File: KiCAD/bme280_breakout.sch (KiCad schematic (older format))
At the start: 8 parts, among them J1 2JUMPER, J2 2JUMPER, P1 CONN_4, U1 BME280

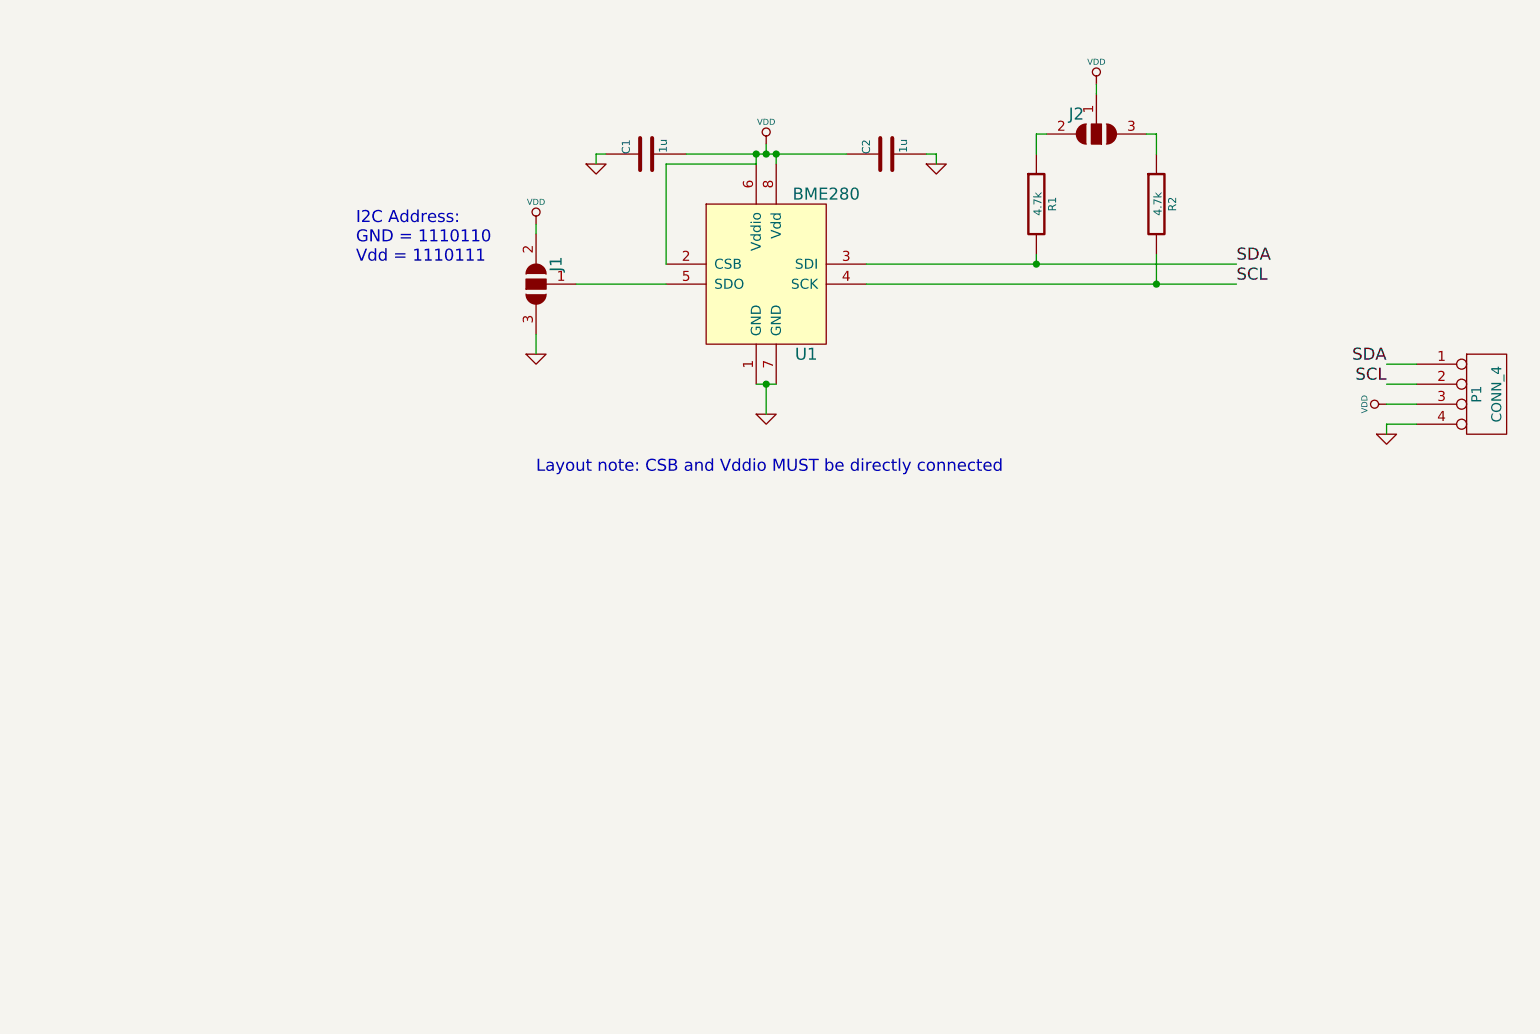
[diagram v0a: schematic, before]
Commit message: Update documentation and clean up repo
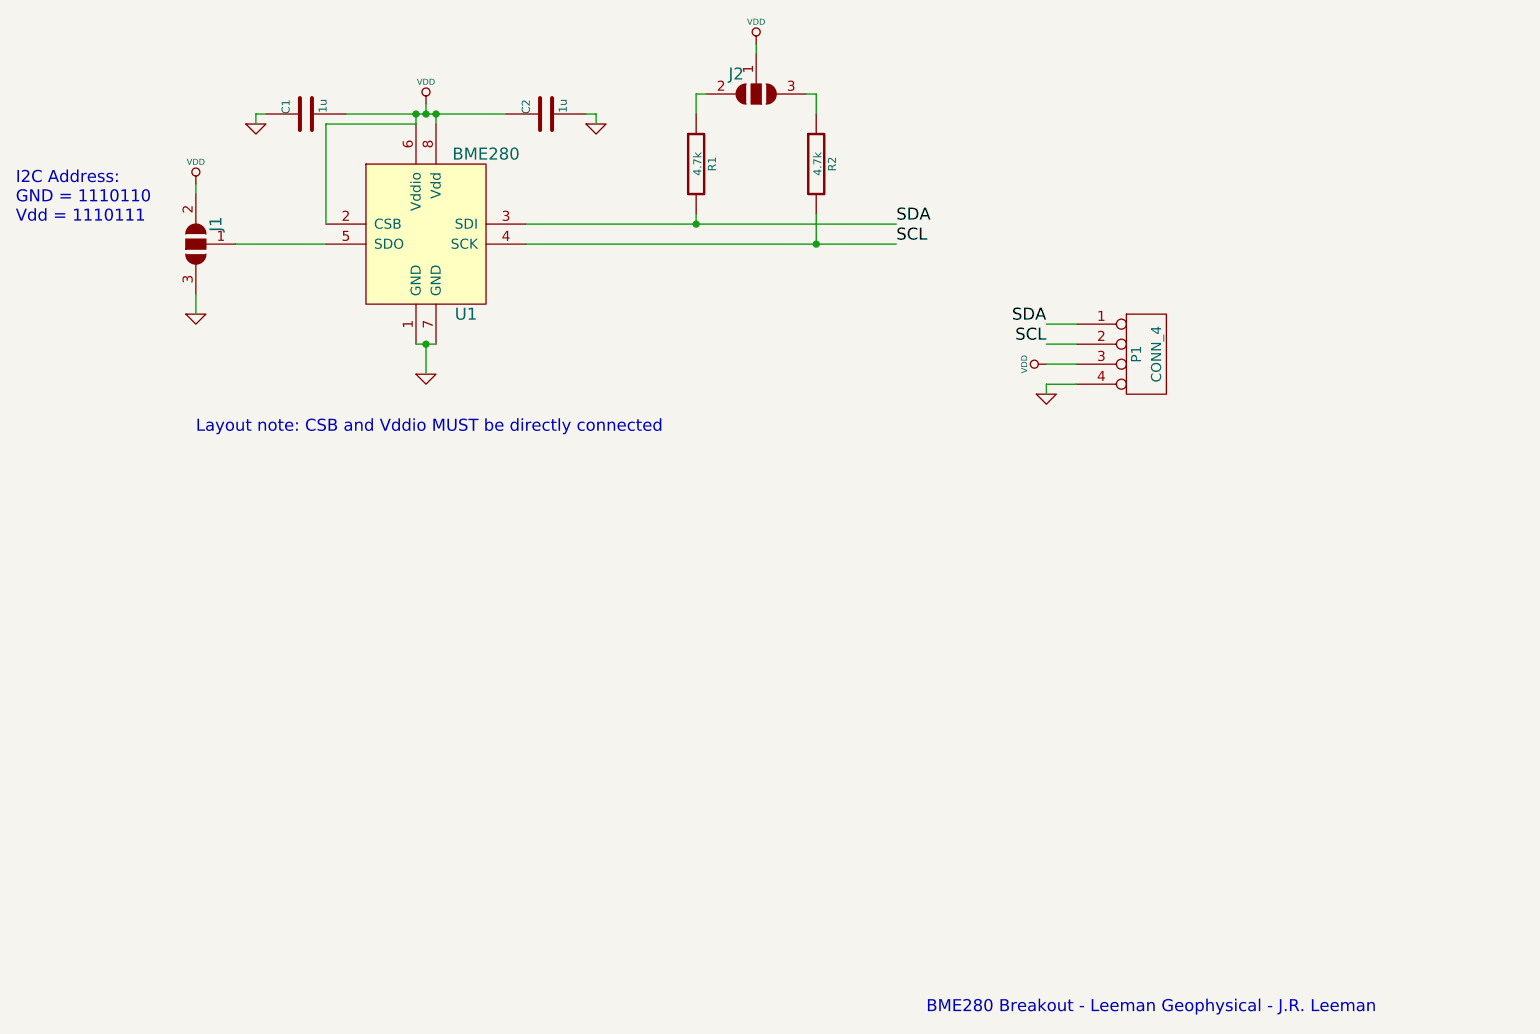
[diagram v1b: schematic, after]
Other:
- note added: "BME280 Breakout - Leeman Geophysical - J.R. Leeman"
- moved on the sheet: C1, C2, J1, J2, P1, R1, R2, U1
